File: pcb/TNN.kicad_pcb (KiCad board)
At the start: 2 copper layers, 43.2 x 33 mm, 6 parts, among them P1 CONN_01X10, P2 CONN_01X04, P3 CONN_01X10, P4 CONN_01X04, SW1 SPST

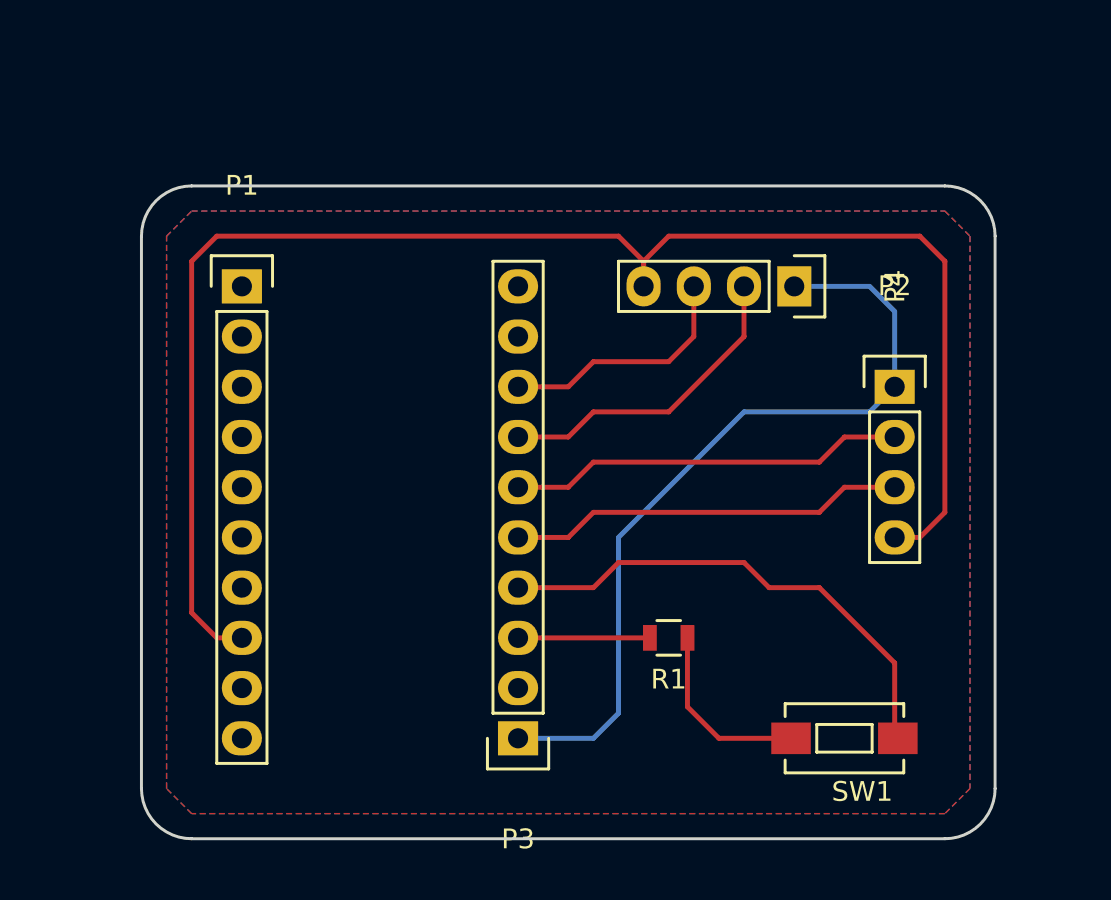
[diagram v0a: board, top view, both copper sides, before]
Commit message: [*] move left (1x10 head pins) 7*.05 inches.
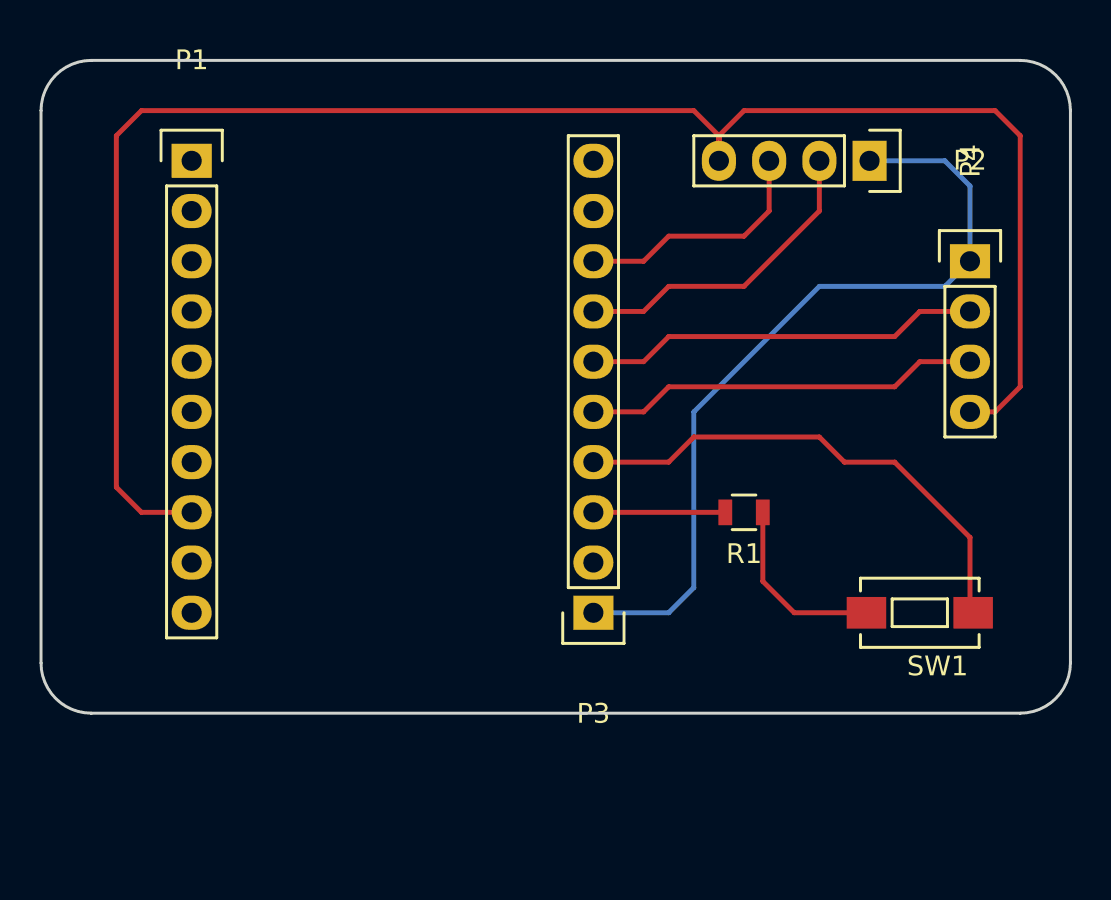
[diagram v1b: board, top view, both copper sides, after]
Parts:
- moved P3 7.41 mm to (45.7, 45.7)
- moved R1 7.41 mm to (53.3, 40.6)
- moved P4 7.41 mm to (59.7, 22.9)
- moved SW1 7.41 mm to (62.2, 45.7)
- moved P2 7.41 mm to (64.8, 27.9)
- moved P1 6.84 mm to (25.4, 22.9)
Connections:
- net +5V renamed V+
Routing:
- net V+: track 79.4 -> 90.8 mm
- removed copper zone on F.Cu, net 3V
- removed copper zone on B.Cu, net GND
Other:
- board size 43.2 x 33 mm -> 52.1 x 33 mm

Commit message: [*] Flip over.
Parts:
- removed P2: CONN_01X04, Pin_Headers:Pin_Header_Straight_1x04
- moved SW1 189.8 mm to (-80.0, -80.0)
- moved P3 186.1 mm to (-91.4, -80.0), turned to 0 degrees
- moved R1 175.8 mm to (-81.3, -72.4), turned to 0 degrees
- moved P1 158.8 mm to (-111.8, -57.1), turned to 180 degrees
- moved P4 158.5 mm to (-72.4, -64.8), turned to 0 degrees
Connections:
- net CLOCK renamed 4-CLOCK
- net DATA renamed 5-DATA
- P3 pad 5: CD -> Net-(P3-Pad5)
- P3 pad 6: CC -> Net-(P3-Pad6)
- R1 pad 1: Net-(R1-Pad1) -> 15
- R1 pad 2: VCC -> GND
- SW1 pad 2: Net-(R1-Pad1) -> VCC
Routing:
- net CD: track 20.1 -> 0.00 mm
- net CC: track 20.1 -> 0.00 mm
- net V+: track 90.8 -> 72.7 mm
- net GND: track 41.0 -> 51.2 mm
- net Net-(R1-Pad1): track 9.39 -> 0.00 mm
- net 5-DATA: track 12.5 -> 20.1 mm
- net VCC: track 6.67 -> 10.8 mm
- net 4-CLOCK: track 16.1 -> 20.1 mm
- net 15: track 25.6 -> 24.7 mm
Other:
- net class 0.4 added: clearance 0.2, trace_width 0.4, via_dia 0.6, via_drill 0.32
